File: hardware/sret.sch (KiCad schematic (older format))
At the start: 0 parts

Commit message: sch update
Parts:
- added ADC1: CONN_01X08, symbol CONN_01X08
- added CON1: SD_Card, 10067847-001, symbol SD_Card
- added EMC1, GPIO1: CONN_02X20, symbol CONN_02X20
- added FB1, FB2: FILTER, symbol FILTER
- added JTAG1: CONN_02X03, symbol CONN_02X03
- added P1: USB_OTG, symbol USB_OTG
- added P2, P? (x3): CONN_02X01, symbol CONN_02X01
- added P6, P? (x3): CONN_01X06, symbol CONN_01X06
- added R1: 12k, symbol R
- added R10, R11, R12, R2, R3, R4, R5, R6: 10k, symbol R
- added R7, R8, R9: 1k5, symbol R
- added R? (x8): 1k5, Resistors_SMD:R_0402, symbol R
- added SGPIO1: CONN_02X08, symbol CONN_02X08
- added U1: LPC4330, symbol LPC4330
- added U2: DRTR5V0U2SR, symbol DRTR5V0U2SR
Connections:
- net labels added: ADC0, ADC1, ADC2, ADC3, ADC4, ADC5, ADC6, ADC7, ADC[0], ADC[1], CAN1_RD, CAN1_TD, DAC, DBGEN, EMC_A0, EMC_A1, EMC_A10, EMC_A11, EMC_A12, EMC_A13, EMC_A14, EMC_A15, EMC_A2, EMC_A3, EMC_A4, EMC_A5, EMC_A6, EMC_A7, EMC_A8, EMC_A9, EMC_BLS0#, EMC_BLS1#, EMC_D0, EMC_D10, EMC_D11, EMC_D12, EMC_D13, EMC_D14, EMC_D15, EMC_D2, EMC_D3, EMC_D4, EMC_D5, EMC_D7, EMC_D8, EMC_D9, EMC_OE#, EMC_WE#, ENET_RXD1, ENET_TX_EN, GND, GPIO0, GPIO1, GPIO10, GPIO11, GPIO2, GPIO3, GPIO4, GPIO5, GPIO6, GPIO7, GPIO8, GPIO9, GP_CLKIN, SD_CD/EMC_D6, SD_CLK, SD_CMD/EMC_CS0#, SD_DATA0/EMC_D1, TCK, TDI, TDO, TMS, TRST#, U0_RX, U0_TX, U1_RX, U1_TX, U2_RX, U2_TX, U3_RX, U3_TX, VCC, XTAL1, XTAL2
- wire segments 0 -> 91
- no-connect marks 0 -> 14

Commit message: alpha alpha schematic
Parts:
- removed ADC1: CONN_01X08, symbol CONN_01X08
- added C1, C? (x13): 100nF, symbol C
- added C10, C11, C2, C6, C? (x2): 18pF, symbol C
- added C12, C13, C? (x4): C, symbol C
- added C?: 10uF, symbol C
- added J?: RJ45-TRANSFO, symbol RJ45-TRANSFO
- added P? (x2): CONN_02X01, symbol CONN_02X01
- added P?: USB_OTG, symbol USB_OTG
- added P?: CONN_02X04, symbol CONN_02X04
- added R13, R14, R15, R16, R17, R? (x2): 10k, symbol R
- added R? (x2): 270, symbol R
- added R?: R, symbol R
- added SW1: DFU, symbol SW_PUSH
- added SW3: RESET, symbol SW_PUSH
- added U3: W25Q80BV, symbol W25Q80BV
- added U? (x2): MAX3051, symbol MAX3051
- added U?: LAN8742A, symbol LAN8742A
- added Y1: RTC, symbol Crystal
- added Y2: 12MHz, symbol Crystal
- added Y?: 25MHz, symbol Crystal
- EMC1, GPIO1: footprint (none) -> Pin_Headers:Pin_Header_Straight_2x20
- gave numbers to parts that had none: 14
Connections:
- net labels added: ALARM, BOOT0/SSPO_MISO/EMC_A6, BOOT1/SSGPIO6/SSPO_MOSI/EMC_A7, BOOT2/SGPIO12/EMC_A8, BOOT3/EMC_A0, CAN0_RXD, CAN0_TXD, CAN1_RXD, CAN1_TXD, CANH_0, CANH_1, CANL_0, CLK0(OUT), ENET_CRS, ENET_MDC, ENET_MDIO, ENET_REF_CLK, ENET_RXDO, ENET_TXD0, ENET_TXD1, ENET_XTAL1, ENET_XTAL2, GPIO12, GPIO13, GPIO14, GPIO15, GPIO16, MISO, MOSI, RESET#, RTC1, RTC2, SCK, SCL, SCL1/SGPIO10, SDA, SDA_1/SGPIO9, SGPIO0, SGPIO1/EMC_A13, SGPIO11, SGPIO2/EMC_A12, SGPIO3/EMC_A11, SGPIO4/EMC_A10, SGPIO5, SGPIO7/SSP1_MISO/EMC_OE#, SGPIO8/SSP1_MOSI/EMC_BLS0#, SIO2, SIO3, SPIFI_CS, SPIO_SEL/EMC_A5, SSP1_SCK, SSPO_CLK, U0_RXD, U0_TXD, U1_RXD/EMC_D11, U1_RXD/EMMC_D10, U2_RXD, U2_TXD, VBAT, WAKEUP
- net labels removed: ADC[0], ADC[1], CAN1_RD, CAN1_TD, EMC_A0, EMC_A10, EMC_A11, EMC_A12, EMC_A13, EMC_A5, EMC_A6, EMC_A7, EMC_A8, EMC_BLS0#, EMC_D10, EMC_D11, EMC_OE#, U1_RX, U1_TX
- wire segments 91 -> 211
- no-connect marks 14 -> 17
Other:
- moved on the sheet: CON1, EMC1, GPIO1, JTAG1, P2, P3, P4, P5, P6, P7, P8, P9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

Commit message: sch update
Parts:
- added C28: 1uF, symbol C
- added FB3: FILTER, symbol FILTER
- added R31, R32, R33, R34: 49.9, Resistors_SMD:R_0603_HandSoldering, symbol R
- added U7: TC1262, TO_SOT_Packages_SMD:SOT-223, symbol TC1262
- C1, C10, C11, C2, C6: footprint (none) -> Capacitors_SMD:C_0603_HandSoldering
- C12, C13: value C -> 100nF; footprint (none) -> Capacitors_SMD:C_0603_HandSoldering
- C14, C15, C16, C17, C19, C21, C22, C23, C26, C3, C4, C5, C7, C8, C9: renamed from C?; footprint (none) -> Capacitors_SMD:C_0603_HandSoldering
- C18, C20: renamed from C?; value C -> 100nF; footprint (none) -> Capacitors_SMD:C_0603_HandSoldering
- C24: renamed from C?; value C -> 1uF; footprint (none) -> Capacitors_SMD:C_0603_HandSoldering
- C25: renamed from C?; value C -> 470pF; footprint (none) -> Capacitors_SMD:C_0603_HandSoldering
- R1, R10, R11, R12, R13, R14, R15, R16, R17, R2, R3, R4, R5, R6, R7, R8, R9: footprint (none) -> Resistors_SMD:R_0603_HandSoldering
- R18, R19, R20, R21, R22, R23, R24, R25: footprint Resistors_SMD:R_0402 -> Resistors_SMD:R_0603_HandSoldering
- R26, R27, R28, R30: renamed from R?; footprint (none) -> Resistors_SMD:R_0603_HandSoldering
- R29: renamed from R?; value R -> 12.1k; footprint (none) -> Resistors_SMD:R_0603_HandSoldering
- gave numbers to parts that had none: 10
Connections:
- net CANH_0: now also GPIO1.19 (P19)
- net CANH_1: now also GPIO1.20 (P20)
- net CANL_0: now also GPIO1.21 (P21), GPIO1.22 (P22)
- net GND: now also GPIO1.23 (P23), J1.13 (SHIELD), P11.6 (shield), C28.2, U7.2 (GND)
- net GPIO16: now also CON1.11 (WRITE_PROTECT), R7.2
- net SD_CD/EMC_D6: now also CON1.10 (CARD_DETECT); no longer R7.2
- net VCC: now also C28.1, FB3.1, U7.3 (Vout)
- net 5V: now reaches FB2.2, R2.1, U1.21 (USB0_VBUS)
- net 5V: now also U7.1 (Vin)
- net at FB1.1, P1.5 (GND): now also P1.6 (shield)
- net at J1.3 (TD-), U4.20 (TXN): now also R33.2
- net at J1.1 (TD+), U4.21 (TXP): now also R34.2
- net at J1.6 (RD-), U4.22 (RXN): now also R31.2
- net at J1.4 (RD+), U4.23 (RXP): now also R32.2
- net EMC_WE# renamed SD_CMD/EMC_WE#
- net SD_CMD/EMC_WE#: now also R8.2
- net SD_CMD/EMC_CS0# renamed SD_POW/EMC_CS0#
- net SD_POW/EMC_CS0#: no longer R8.2
- new net: FB3.2, R31.1, R32.1, R33.1, R34.1
- no-connect marks 17 -> 15
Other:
- moved on the sheet: CON1, J1, R10, R11, R12, R7, R8, R9, SGPIO1

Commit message: lpc4330 footprint
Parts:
- removed R12: 10k, Resistors_SMD:R_0603_HandSoldering, symbol R
- removed Y2: 12MHz, symbol Crystal
- removed Y3: 25MHz, symbol Crystal
- added D1, D2: LED, Resistors_SMD:R_0603_HandSoldering, symbol LED
- added X1, X2: CRYSTAL_SMD, Crystals:crystal_FA238-TSX3225, symbol CRYSTAL_SMD
- C27, C28: footprint (none) -> Capacitors_SMD:C_0603_HandSoldering
- CON1: footprint 10067847-001 -> Connect:SD_Card_Receptacle
- FB1, FB2, FB3: footprint (none) -> Resistors_SMD:R_0805_HandSoldering
- JTAG1: footprint (none) -> Socket_Strips:Socket_Strip_Straight_2x03
- P1: value USB_OTG -> USB0; footprint (none) -> Connect:USB_Micro-B
- P10: footprint (none) -> Pin_Headers:Pin_Header_Straight_2x04
- P11: value USB_OTG -> USB1; footprint (none) -> Connect:USB_Micro-B
- P12, P13, P2, P3, P4, P5: footprint (none) -> Pin_Headers:Pin_Header_Straight_2x01
- P6, P7, P8, P9: footprint (none) -> Pin_Headers:Pin_Header_Straight_1x06
- R10: value 10k -> 1.5k
- R11: value 10k -> 1k5
- R7: value 1k5 -> 1.5k
- SGPIO1: footprint (none) -> Socket_Strips:Socket_Strip_Straight_2x08
- U2: footprint (none) -> TO_SOT_Packages_SMD:SOT-143
- U3: footprint (none) -> SMD_Packages:SOIC-8-N
- U5, U6: footprint (none) -> lib:sot-23-8
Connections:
- net 5V: now also P11.1 (VCC)
- net ENET_XTAL1: now also C22.1, X2.1
- net ENET_XTAL2: now also C23.1, X2.2
- net GND: now also R7.2, X1.3 (case), X2.3 (case); no longer R10.2, R11.2
- net GPIO16: now also R10.2; no longer R7.2
- net RTC1: now also C2.1
- net RTC2: now also C6.1
- net SD_DATA0/EMC_D1: now also R11.2; no longer CON1.7 (DAT0)
- net SGPIO11: no longer U1.91 (SGPIO14)
- net VCC: now also U1.71 (VDDIO), D1.2 (A), D2.2 (A)
- net XTAL1: now also C10.1, X1.1
- net XTAL2: now also C11.1, X1.2
- net at CON1.1 (CD/DAT3): no longer R7.1
- net at CON1.2 (CMD), R8.1: no longer R11.1
- net at CON1.5 (CLK), R9.1: no longer R10.1
- new net: CON1.7 (DAT0), R11.1
- new net: D1.1 (K), R7.1
- new net: D2.1 (K), R10.1
- new net SGPIO11/USB1_VBUS: U1.91 (SGPIO14)
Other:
- note added: "Not sure if SD lines need pull-up/down resistors."
- moved on the sheet: C10, C11, C2, C22, C6

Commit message: almost finised with footprint
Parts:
- J1: footprint (none) -> Connect:RJ45_TRANSFO
- JTAG1: footprint Socket_Strips:Socket_Strip_Straight_2x03 -> Connect:RJ45_TRANSFO
- U1: footprint (none) -> lib:lqfp144
- U4: footprint (none) -> Housings_DFN_QFN:QFN-24-1EP_4x4mm_Pitch0.5mm
- Y1: footprint (none) -> lib:rtc
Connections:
- net GND: now also U4.25 (GND)
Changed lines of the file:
@@
 F 0 "U1" H 5200 3550 39  0000 C CNN
 F 1 "LPC4330" H 5200 3700 60  0000 C CNN
-F 2 "" H 5300 900 60  0001 C CNN
+F 2 "lib:lqfp144" H 5300 900 60  0001 C CNN
 F 3 "http://www.nxp.com/documents/user_manual/UM10503.pdf" H 5300 900 60  0001 C CNN
 	1    5200 3750
@@
 F 0 "JTAG1" H 15550 4050 50  0000 C CNN
 F 1 "CONN_02X03" H 15550 3650 50  0000 C CNN
-F 2 "Socket_Strips:Socket_Strip_Straight_2x03" H 15550 2650 50  0001 C CNN
+F 2 "Connect:RJ45_TRANSFO" H 15550 2650 50  0001 C CNN
 F 3 "" H 15550 2650 50  0000 C CNN
 	1    15550 3850
@@
 F 0 "Y1" H 1250 10000 50  0000 C CNN
 F 1 "RTC" H 1250 9700 50  0000 C CNN
-F 2 "" H 1250 9850 50  0001 C CNN
+F 2 "lib:rtc" H 1250 9850 50  0001 C CNN
 F 3 "http://www.abracon.com/Support/PackageDrawing/Resonators/AB26TRQ.PDF" H 1250 9850 50  0001 C CNN
 	1    1250 9850
@@
 F 0 "U4" H 10050 8100 60  0000 C CNN
 F 1 "LAN8742A" H 10050 7800 60  0000 C CNN
-F 2 "" H 10050 7800 60  0001 C CNN
+F 2 "Housings_DFN_QFN:QFN-24-1EP_4x4mm_Pitch0.5mm" H 10050 7800 60  0001 C CNN
 F 3 "http://ww1.microchip.com/downloads/en/DeviceDoc/8742a.pdf" H 10050 7800 60  0001 C CNN
 	1    10050 8000
@@
 F 0 "J1" H 6250 9600 50  0000 L CNN
 F 1 "RJ45-TRANSFO" H 6100 9600 50  0000 R CNN
-F 2 "" H 6150 9000 50  0001 C CNN
-F 3 "http://www.digikey.com/product-detail/en/abracon-llc/ARJC02-111008B/535-12605-ND/4696789" H 6150 9000 50  0001 C CNN
+F 2 "Connect:RJ45_TRANSFO" H 6150 9000 50  0001 C CNN
+F 3 "http://www.digikey.com/product-detail/en/abracon-llc/ARJC01-111002AR/535-12602-ND/4696786" H 6150 9000 50  0001 C CNN
 	1    6150 9000
 	-1   0    0    1
@@
 Wire Wire Line
 	10050 9900 10050 9850
+$Comp
+L GND #PWR?
+U 1 1 58CB8592
+P 11150 8500
+F 0 "#PWR?" H 11150 8250 50  0001 C CNN
+F 1 "GND" H 11150 8350 50  0000 C CNN
+F 2 "" H 11150 8500 50  0000 C CNN
+F 3 "" H 11150 8500 50  0000 C CNN
+	1    11150 8500
+	1    0    0    -1
+$EndComp
+Wire Wire Line
+	11100 8500 11150 8500
 $EndSCHEMATC

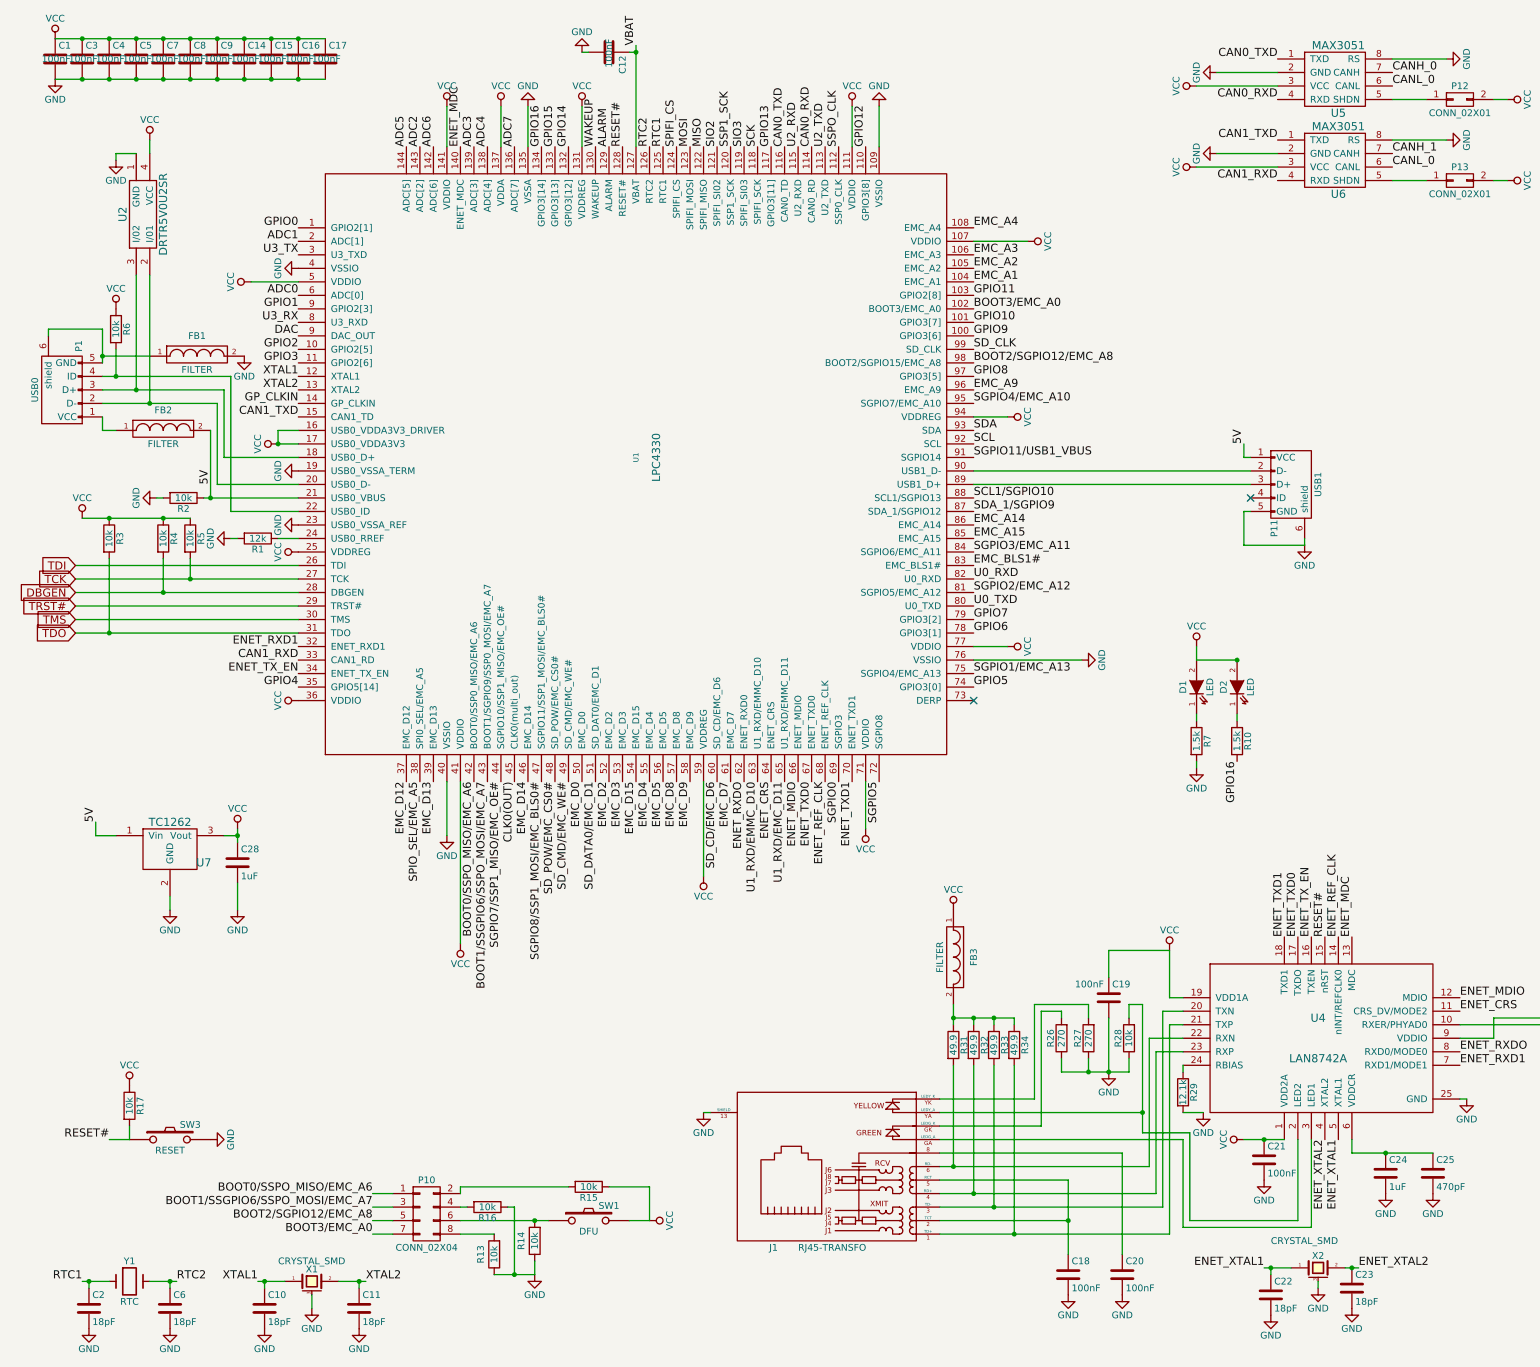
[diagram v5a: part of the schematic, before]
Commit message: footprint finished, starting PCB
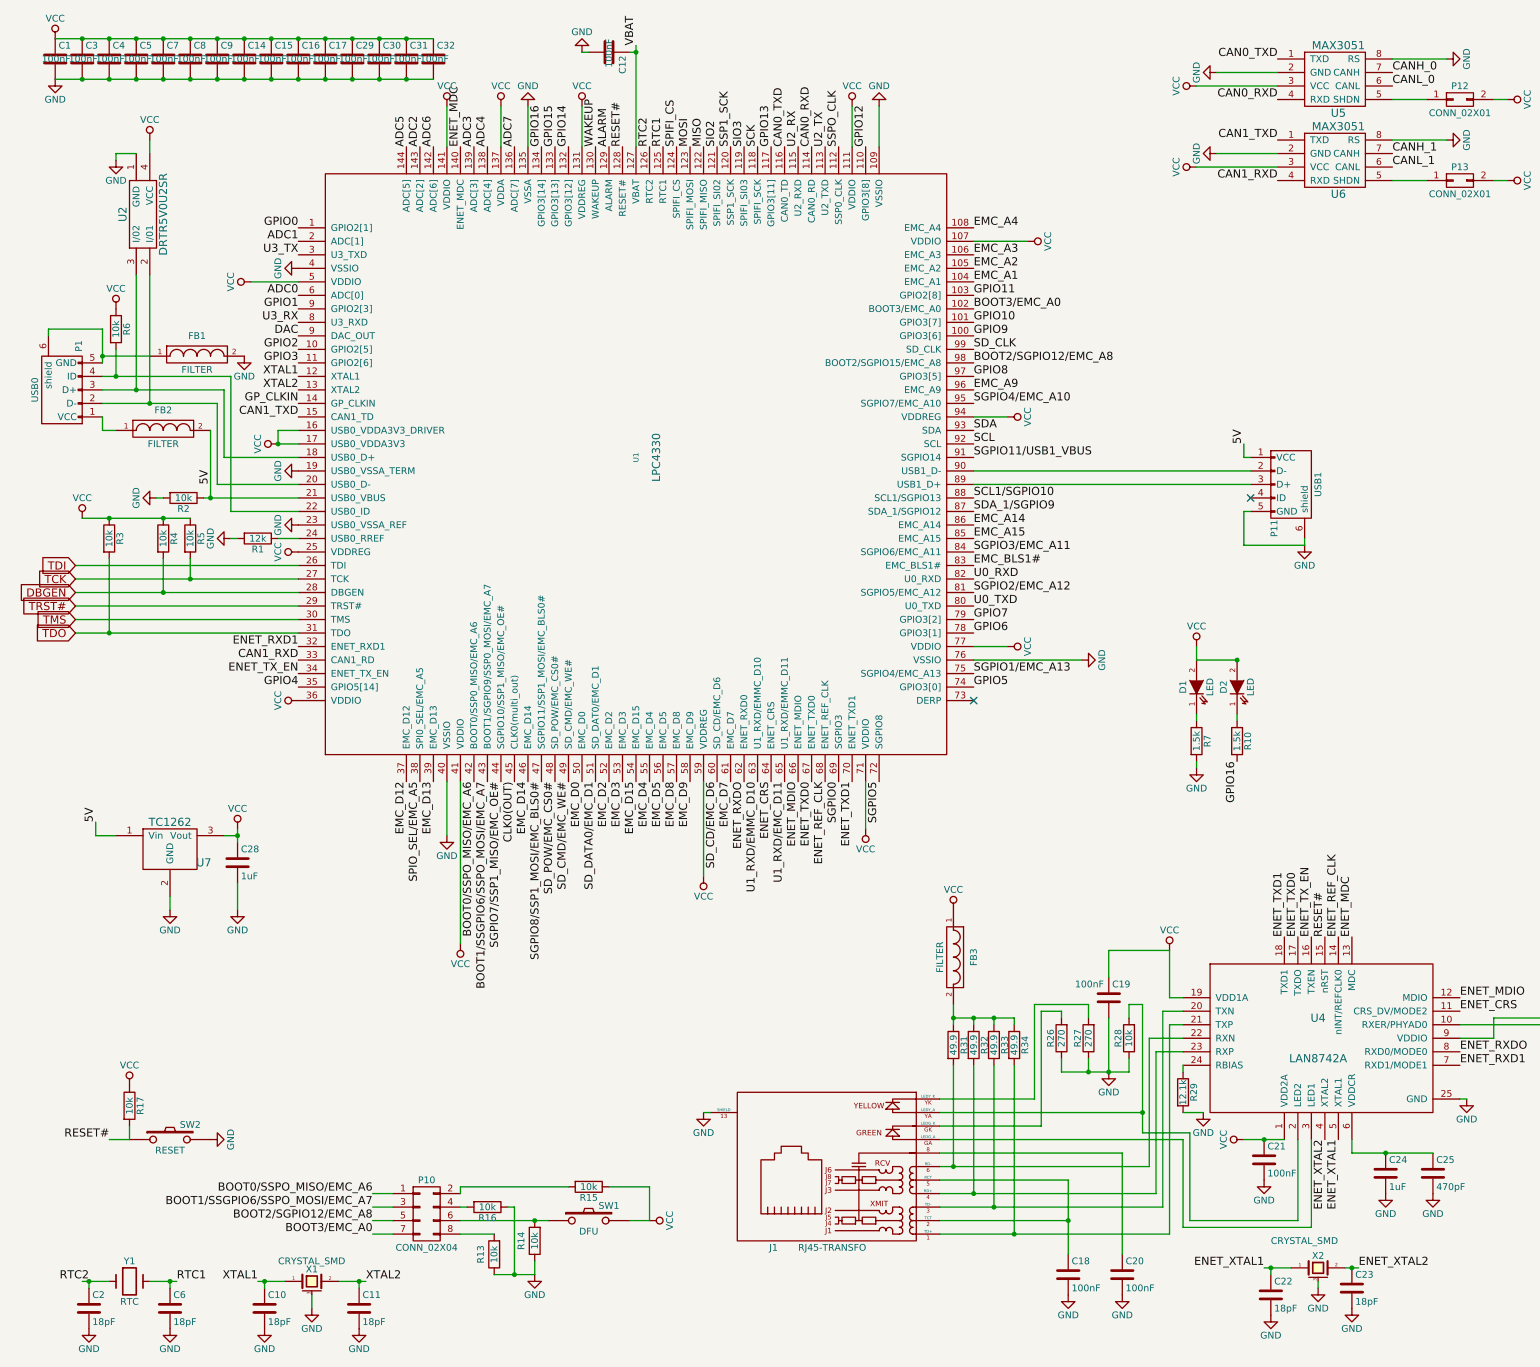
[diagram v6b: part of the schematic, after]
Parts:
- added C29, C30, C31, C32: 100nF, Capacitors_SMD:C_0603_HandSoldering, symbol C
- EMC1, GPIO1: footprint Pin_Headers:Pin_Header_Straight_2x20 -> Socket_Strips:Socket_Strip_Straight_2x20
- JTAG1: footprint Connect:RJ45_TRANSFO -> Socket_Strips:Socket_Strip_Straight_2x03
- SW1: footprint (none) -> lib:button
- SW2: renamed from SW3; footprint (none) -> lib:button
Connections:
- net U2_RXD is gone; now on net U2_RX: U1.115 (U2_RXD)
- net U2_TXD is gone; now on net U2_TX: U1.113 (U2_TXD)
- net CANL_0: no longer U6.6 (CANL)
- net GND: now also C29.2, C30.2, C31.2, C32.2
- net RTC1: now also C6.1, Y1.2; no longer C2.1, Y1.1
- net RTC2: now also C2.1, Y1.1; no longer C6.1, Y1.2
- net VCC: now also C29.1, C30.1, C31.1, C32.1
- new net CANL_1: U6.6 (CANL)
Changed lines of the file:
@@
 F 0 "GPIO1" H 13500 2650 50  0000 C CNN
 F 1 "CONN_02X20" V 13500 1600 50  0000 C CNN
-F 2 "Pin_Headers:Pin_Header_Straight_2x20" H 13500 650 50  0001 C CNN
+F 2 "Socket_Strips:Socket_Strip_Straight_2x20" H 13500 650 50  0001 C CNN
 F 3 "" H 13500 650 50  0000 C CNN
 	1    13500 1600
@@
 F 0 "EMC1" H 13500 4800 50  0000 C CNN
 F 1 "CONN_02X20" V 13500 3750 50  0000 C CNN
-F 2 "Pin_Headers:Pin_Header_Straight_2x20" H 13500 2800 50  0001 C CNN
+F 2 "Socket_Strips:Socket_Strip_Straight_2x20" H 13500 2800 50  0001 C CNN
 F 3 "" H 13500 2800 50  0000 C CNN
 	1    13500 3750
@@
 F 0 "JTAG1" H 15550 4050 50  0000 C CNN
 F 1 "CONN_02X03" H 15550 3650 50  0000 C CNN
-F 2 "Connect:RJ45_TRANSFO" H 15550 2650 50  0001 C CNN
+F 2 "Socket_Strips:Socket_Strip_Straight_2x03" H 15550 2650 50  0001 C CNN
 F 3 "" H 15550 2650 50  0000 C CNN
 	1    15550 3850
@@
 EMC_A4
 Text Label 6400 1450 1    60   ~ 0
-U2_TXD
+U2_TX
 Text Label 6200 1450 1    60   ~ 0
-U2_RXD
+U2_RX
 Text Label 4700 1450 1    60   ~ 0
 WAKEUP
@@
 RESET#
 $Comp
-L SW_PUSH SW3
+L SW_PUSH SW2
 U 1 1 58D06D7A
 P 1550 8800
-F 0 "SW3" H 1700 8910 50  0000 C CNN
+F 0 "SW2" H 1700 8910 50  0000 C CNN
 F 1 "RESET" H 1550 8720 50  0000 C CNN
-F 2 "" H 1550 8800 50  0001 C CNN
+F 2 "lib:button" H 1550 8800 50  0001 C CNN
 F 3 "" H 1550 8800 50  0000 C CNN
 	1    1550 8800
@@
 Text Label 5200 1450 1    60   ~ 0
 RTC1
-Text Label 900  9850 2    60   ~ 0
-RTC1
 Text Label 1600 9850 0    60   ~ 0
+RTC1
+Text Label 950  9850 2    60   ~ 0
 RTC2
 $Comp
@@
 F 0 "SW1" H 4800 9510 50  0000 C CNN
 F 1 "DFU" H 4650 9320 50  0000 C CNN
-F 2 "" H 4650 9400 50  0001 C CNN
+F 2 "lib:button" H 4650 9400 50  0001 C CNN
 F 3 "" H 4650 9400 50  0000 C CNN
 	1    4650 9400
@@
 CANH_0
 Text Label 10600 1600 0    60   ~ 0
-CANL_0
+CANL_1
 Text Label 13250 1550 2    60   ~ 0
 CANH_0
@@
 Connection ~ 1700 650
 Wire Wire Line
-	700  650  2700 650
+	700  650  3500 650
 Connection ~ 900  950
 Connection ~ 1100 950
@@
 Connection ~ 1700 950
 Wire Wire Line
-	700  950  2700 950
+	700  950  3500 950
 Wire Wire Line
 	2400 9850 2200 9850
@@
 	10050 9900 10050 9850
 $Comp
-L GND #PWR?
+L GND #PWR088
 U 1 1 58CB8592
 P 11150 8500
-F 0 "#PWR?" H 11150 8250 50  0001 C CNN
+F 0 "#PWR088" H 11150 8250 50  0001 C CNN
 F 1 "GND" H 11150 8350 50  0000 C CNN
 F 2 "" H 11150 8500 50  0000 C CNN
@@
 Wire Wire Line
 	11100 8500 11150 8500
+$Comp
+L C C29
+U 1 1 58CCCA62
+P 2900 800
+F 0 "C29" H 2925 900 50  0000 L CNN
+F 1 "100nF" H 2800 800 50  0000 L CNN
+F 2 "Capacitors_SMD:C_0603_HandSoldering" H 2938 650 50  0001 C CNN
+F 3 "" H 2900 800 50  0000 C CNN
+	1    2900 800
+	1    0    0    -1
+$EndComp
+$Comp
+L C C30
+U 1 1 58CCCBA0
+P 3100 800
+F 0 "C30" H 3125 900 50  0000 L CNN
+F 1 "100nF" H 3000 800 50  0000 L CNN
+F 2 "Capacitors_SMD:C_0603_HandSoldering" H 3138 650 50  0001 C CNN
+F 3 "" H 3100 800 50  0000 C CNN
+	1    3100 800
+	1    0    0    -1
+$EndComp
+$Comp
+L C C31
+U 1 1 58CCCCE1
+P 3300 800
+F 0 "C31" H 3325 900 50  0000 L CNN
+F 1 "100nF" H 3200 800 50  0000 L CNN
+F 2 "Capacitors_SMD:C_0603_HandSoldering" H 3338 650 50  0001 C CNN
+F 3 "" H 3300 800 50  0000 C CNN
+	1    3300 800
+	1    0    0    -1
+$EndComp
+$Comp
+L C C32
+U 1 1 58CCCE21
+P 3500 800
+F 0 "C32" H 3525 900 50  0000 L CNN
+F 1 "100nF" H 3400 800 50  0000 L CNN
+F 2 "Capacitors_SMD:C_0603_HandSoldering" H 3538 650 50  0001 C CNN
+F 3 "" H 3500 800 50  0000 C CNN
+	1    3500 800
+	1    0    0    -1
+$EndComp
+Connection ~ 3300 950
+Connection ~ 3100 950
+Connection ~ 2700 950
+Connection ~ 2900 950
+Connection ~ 3300 650
+Connection ~ 3100 650
+Connection ~ 2700 650
+Connection ~ 2900 650
 $EndSCHEMATC
